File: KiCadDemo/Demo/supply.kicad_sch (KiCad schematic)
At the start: 13 parts, among them J1 Power, U1 TSR_1-2450, U2 UA78M33

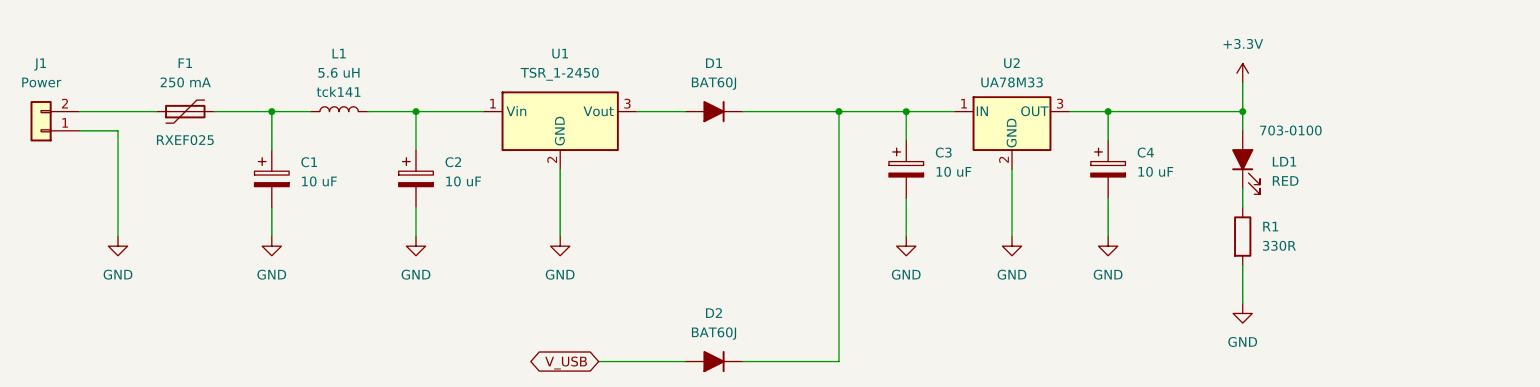
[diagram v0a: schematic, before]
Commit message: check5_placementV2
Replacement of components. Start of the routing
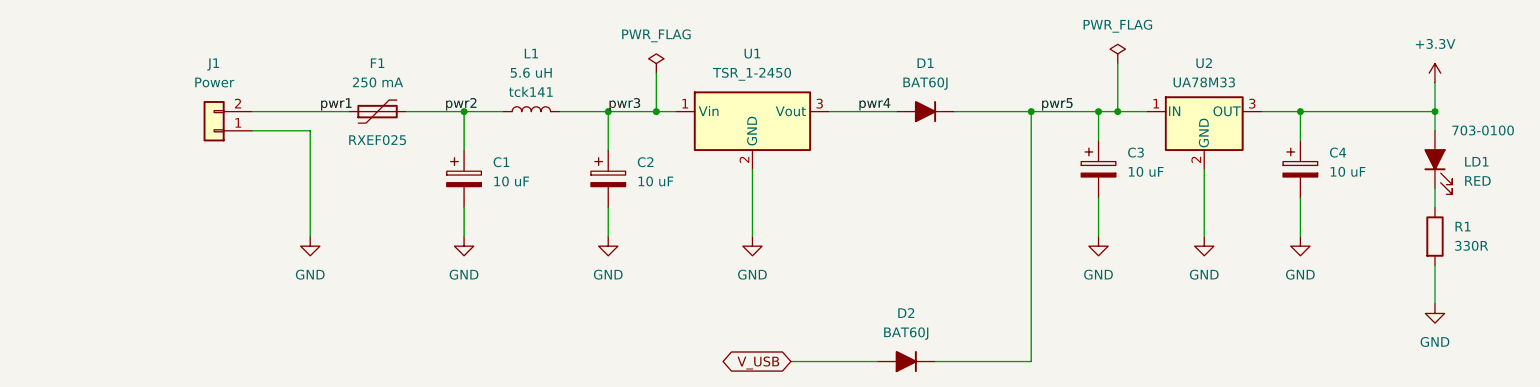
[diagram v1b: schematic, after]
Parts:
- J1: footprint (none) -> Demo:Power
- L1: footprint (none) -> Demo:tck141
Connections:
- net pwr1: now reaches F1.1, J1.2 (Pin_2)
- net pwr2: now reaches C1.1, F1.2, L1.1
- net pwr5: now reaches C3.1, D1.1 (K), D2.1 (K), U2.1 (IN)
- net pwr4: now reaches D1.2 (A), U1.3 (Vout)
- net pwr3: now reaches C2.1, L1.2, U1.1 (Vin)
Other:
- moved on the sheet: C1, C2, C3, C4, D1, D2, F1, J1, L1, LD1, R1, U1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
